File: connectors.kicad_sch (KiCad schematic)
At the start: 3 parts, among them J1 112-024-113R001, J3 RJHSE5380, J4 USB_C_Receptacle_USB2.0_16P

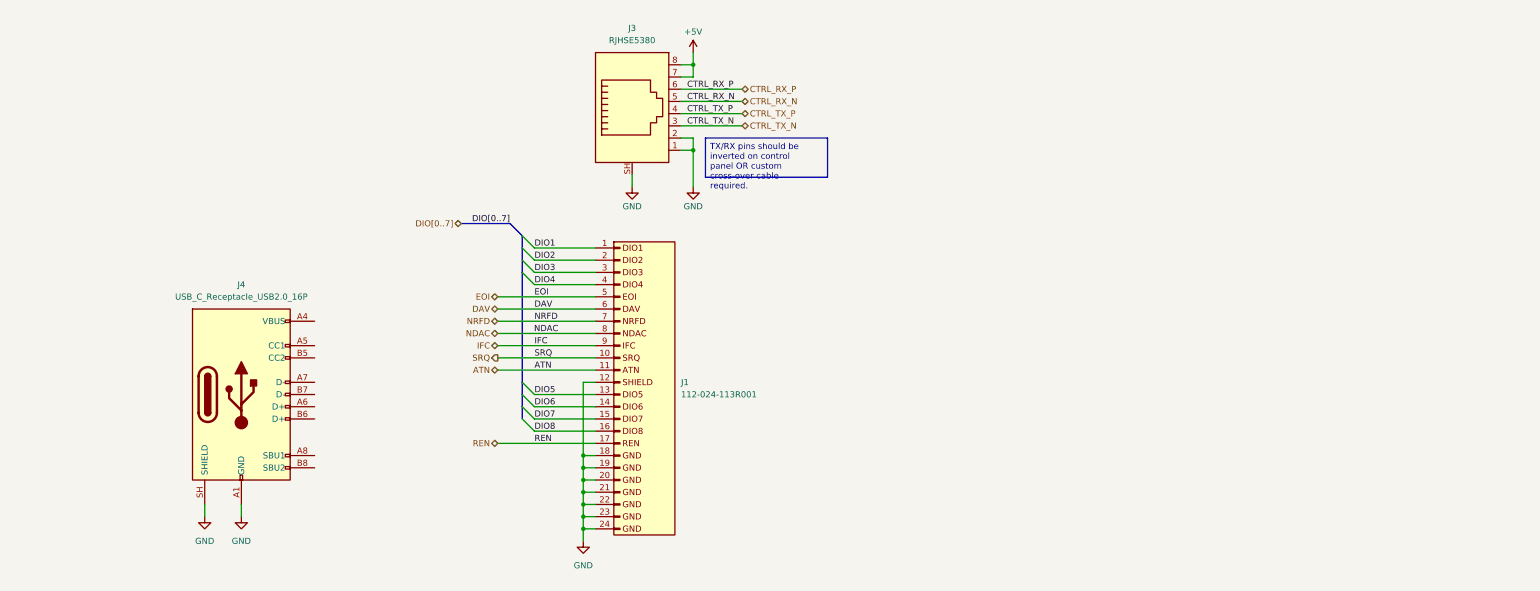
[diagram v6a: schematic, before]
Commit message: Add power supply and USB protection
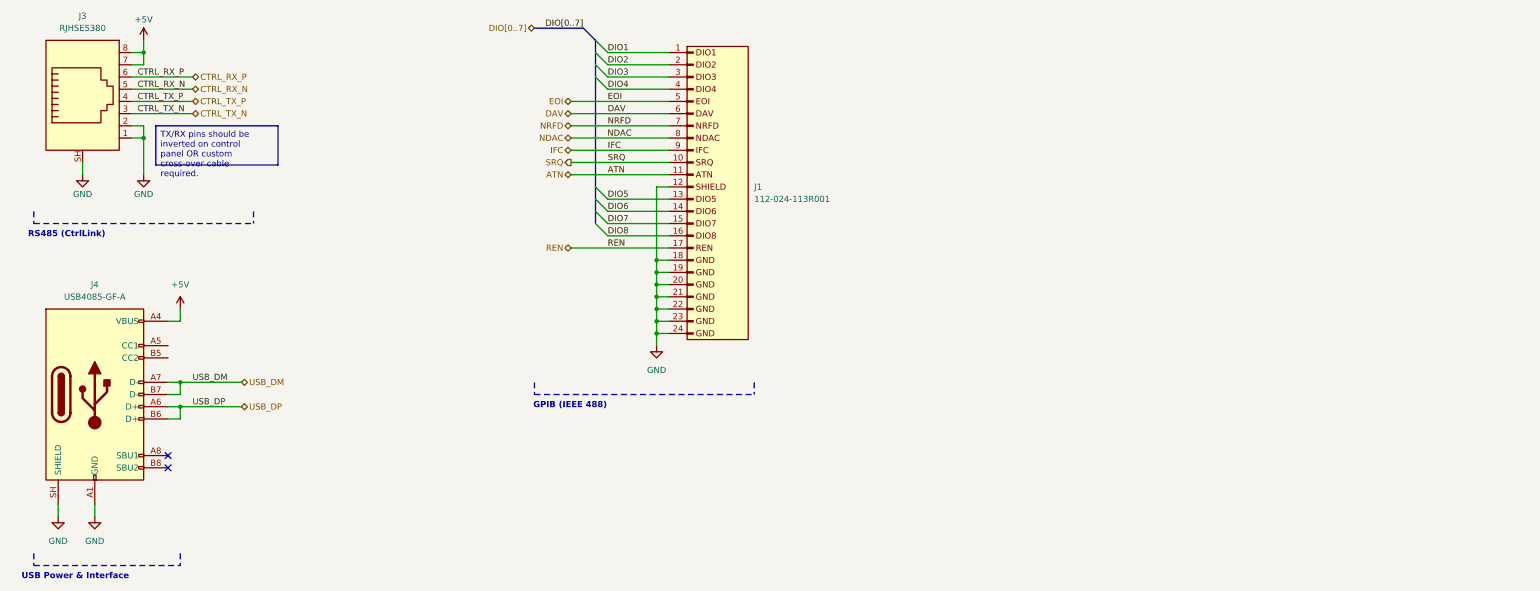
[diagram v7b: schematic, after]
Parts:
- removed J4: USB_C_Receptacle_USB2.0_16P, Connector_USB:USB_C_Receptacle_Amphenol_12401948E412A, symbol Connector:USB_C_Receptacle_USB2.0_16P
- added J4: USB4085-GF-A, Connector_USB:USB_C_Receptacle_GCT_USB4085, symbol PARTSDB:USB4085-GF-A
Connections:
- net +5V: now also J4.A4 (VBUS), J4.A9 (VBUS), J4.B4 (VBUS), J4.B9 (VBUS)
- net GND: now also J4.A1 (GND), J4.A12 (GND), J4.B1 (GND), J4.B12 (GND), J4.SH (SHIELD)
- new net USB_DM: J4.A7 (D-), J4.B7 (D-)
- new net USB_DP: J4.A6 (D+), J4.B6 (D+)
- no-connect marks 0 -> 2
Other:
- note added: "GPIB (IEEE 488)"
- note added: "RS485 (CtrlLink)"
- note added: "USB Power & Interface"
- moved on the sheet: J1, J3

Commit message: Finish up schematics
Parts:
- added R6, R7: 5.1k, Resistor_SMD:R_0603_1608Metric, symbol PARTSDB:RC0603FR-075K1L
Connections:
- net DIO5: now also J1.13 (Pin_13)
- net GND: now also R6.2, R7.2
- net at J4.A5 (CC1): now also R7.1
- net at J4.B5 (CC2): now also R6.1
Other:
- title: (none) -> Connectors
- moved on the sheet: J1, J3, J4
